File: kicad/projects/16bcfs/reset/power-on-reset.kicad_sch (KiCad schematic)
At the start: 2 parts

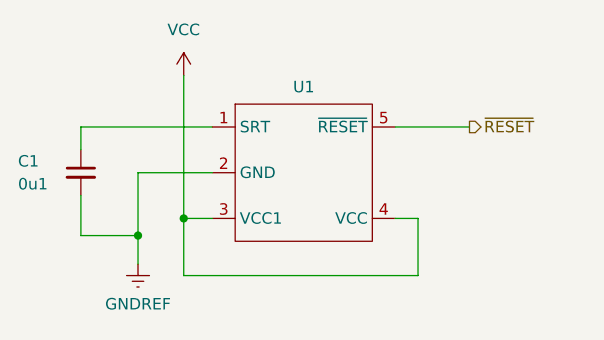
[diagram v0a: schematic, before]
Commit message: Added some debugging code
This is still not working.  I will need to revamp the reset routines for
the emulator to get this to work properly.  Everything will need an
initial state on construction and a `reset()` routine to place
everything into a proper state.  This in itself will be a major change.
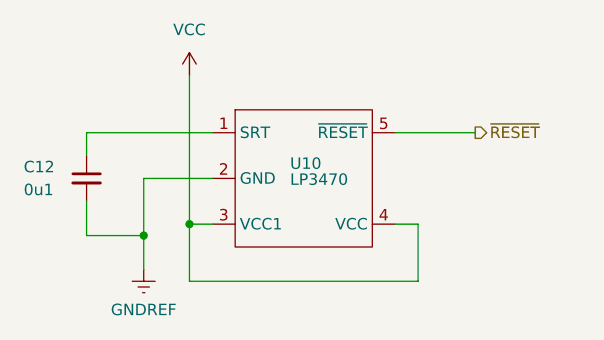
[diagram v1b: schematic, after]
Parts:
- U10: renamed from U1; value ~ -> LP3470
- renumbered C1 to C12
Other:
- moved on the sheet: C12, U10
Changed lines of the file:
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@@
     (comment 1 "Adam Clark (@eryjus)")
   )
-  (junction (at 132.715 104.775) (diameter 0) (color 0 0 0 0)
+  (junction (at 133.35 105.41) (diameter 0) (color 0 0 0 0)
   )
-  (junction (at 127.635 106.68) (diameter 0) (color 0 0 0 0)
+  (junction (at 128.27 106.68) (diameter 0) (color 0 0 0 0)
   )
-  (wire (pts (xy 121.285 106.68) (xy 127.635 106.68))
+  (wire (pts (xy 121.92 106.68) (xy 128.27 106.68))
     (stroke (width 0) (type default))
   )
-  (wire (pts (xy 127.635 99.695) (xy 127.635 106.68))
+  (wire (pts (xy 128.27 100.33) (xy 128.27 106.68))
     (stroke (width 0) (type default))
   )
-  (wire (pts (xy 132.715 111.125) (xy 132.715 104.775))
+  (wire (pts (xy 133.35 111.76) (xy 133.35 105.41))
     (stroke (width 0) (type default))
   )
-  (wire (pts (xy 132.715 104.775) (xy 135.89 104.775))
+  (wire (pts (xy 133.35 105.41) (xy 135.89 105.41))
     (stroke (width 0) (type default))
   )
-  (wire (pts (xy 121.285 102.235) (xy 121.285 106.68))
+  (wire (pts (xy 121.92 102.87) (xy 121.92 106.68))
     (stroke (width 0) (type default))
   )
-  (wire (pts (xy 164.465 94.615) (xy 156.21 94.615))
+  (wire (pts (xy 165.1 95.25) (xy 156.21 95.25))
     (stroke (width 0) (type default))
   )
-  (wire (pts (xy 132.715 88.9) (xy 132.715 104.775))
+  (wire (pts (xy 133.35 88.9) (xy 133.35 105.41))
     (stroke (width 0) (type default))
   )
-  (wire (pts (xy 135.89 94.615) (xy 121.285 94.615))
+  (wire (pts (xy 135.89 95.25) (xy 121.92 95.25))
     (stroke (width 0) (type default))
   )
-  (wire (pts (xy 158.75 111.125) (xy 132.715 111.125))
+  (wire (pts (xy 158.75 111.76) (xy 133.35 111.76))
     (stroke (width 0) (type default))
   )
-  (wire (pts (xy 127.635 106.68) (xy 127.635 109.855))
+  (wire (pts (xy 128.27 106.68) (xy 128.27 110.49))
     (stroke (width 0) (type default))
   )
-  (wire (pts (xy 156.21 104.775) (xy 158.75 104.775))
+  (wire (pts (xy 156.21 105.41) (xy 158.75 105.41))
     (stroke (width 0) (type default))
   )
-  (wire (pts (xy 135.89 99.695) (xy 127.635 99.695))
+  (wire (pts (xy 135.89 100.33) (xy 128.27 100.33))
     (stroke (width 0) (type default))
   )
-  (wire (pts (xy 121.285 94.615) (xy 121.285 97.155))
+  (wire (pts (xy 121.92 95.25) (xy 121.92 97.79))
     (stroke (width 0) (type default))
   )
-  (wire (pts (xy 158.75 104.775) (xy 158.75 111.125))
+  (wire (pts (xy 158.75 105.41) (xy 158.75 111.76))
     (stroke (width 0) (type default))
   )
-  (hierarchical_label "~{RESET}" (shape output) (at 164.465 94.615 0) (fields_autoplaced)
+  (hierarchical_label "~{RESET}" (shape output) (at 165.1 95.25 0) (fields_autoplaced)
     (effects (font (size 1.27 1.27)) (justify left))
   )
-  (symbol (lib_id "eryjus:LP3470A") (at 146.05 99.695 0) (unit 1)
-    (in_bom yes) (on_board yes) (dnp no) (fields_autoplaced)
-    (property "Reference" "U1" (at 146.05 90.17 0)
-      (effects (font (size 1.27 1.27)))
+  (symbol (lib_id "eryjus:LP3470A") (at 146.05 100.33 0) (unit 1)
+    (in_bom yes) (on_board yes) (dnp no)
+    (property "Reference" "U10" (at 144.526 98.679 0)
+      (effects (font (size 1.27 1.27)) (justify left))
     )
-    (property "Value" "~" (at 146.05 99.695 0)
-      (effects (font (size 1.27 1.27)))
+    (property "Value" "LP3470" (at 144.526 100.457 0)
+      (effects (font (size 1.27 1.27)) (justify left))
     )
-    (property "Footprint" "" (at 146.05 99.695 0)
+    (property "Footprint" "" (at 146.05 100.33 0)
       (effects (font (size 1.27 1.27)) hide)
     )
-    (property "Datasheet" "" (at 146.05 99.695 0)
+    (property "Datasheet" "" (at 146.05 100.33 0)
       (effects (font (size 1.27 1.27)) hide)
     )
@@
       (project "reset"
         (path "/d0ae44e5-d74e-4df6-bf3d-e0535c5a7785/bb61786e-9a6f-43f1-ab22-9986a9d0f989"
-          (reference "U1") (unit 1)
+          (reference "U10") (unit 1)
         )
       )
     )
   )
-  (symbol (lib_id "Device:C_Small") (at 121.285 99.695 0) (unit 1)
+  (symbol (lib_id "Device:C_Small") (at 121.92 100.33 0) (unit 1)
     (in_bom yes) (on_board yes) (dnp no)
-    (property "Reference" "C1" (at 114.3 98.425 0)
+    (property "Reference" "C12" (at 114.935 99.06 0)
       (effects (font (size 1.27 1.27)) (justify left))
     )
-    (property "Value" "0u1" (at 114.3 100.965 0)
+    (property "Value" "0u1" (at 114.935 101.6 0)
       (effects (font (size 1.27 1.27)) (justify left))
     )
-    (property "Footprint" "" (at 121.285 99.695 0)
+    (property "Footprint" "" (at 121.92 100.33 0)
       (effects (font (size 1.27 1.27)) hide)
     )
-    (property "Datasheet" "~" (at 121.285 99.695 0)
+    (property "Datasheet" "~" (at 121.92 100.33 0)
       (effects (font (size 1.27 1.27)) hide)
     )
@@
       (project "reset"
         (path "/d0ae44e5-d74e-4df6-bf3d-e0535c5a7785/bb61786e-9a6f-43f1-ab22-9986a9d0f989"
-          (reference "C1") (unit 1)
+          (reference "C12") (unit 1)
         )
       )
     )
   )
-  (symbol (lib_id "power:VCC") (at 132.715 88.9 0) (mirror y) (unit 1)
+  (symbol (lib_id "power:VCC") (at 133.35 88.9 0) (mirror y) (unit 1)
     (in_bom yes) (on_board yes) (dnp no)
-    (property "Reference" "#PWR06" (at 132.715 92.71 0)
+    (property "Reference" "#PWR014" (at 133.35 92.71 0)
       (effects (font (size 1.27 1.27)) hide)
     )
-    (property "Value" "VCC" (at 132.715 83.82 0)
+    (property "Value" "VCC" (at 133.35 83.82 0)
       (effects (font (size 1.27 1.27)))
     )
-    (property "Footprint" "" (at 132.715 88.9 0)
+    (property "Footprint" "" (at 133.35 88.9 0)
       (effects (font (size 1.27 1.27)) hide)
     )
-    (property "Datasheet" "" (at 132.715 88.9 0)
+    (property "Datasheet" "" (at 133.35 88.9 0)
       (effects (font (size 1.27 1.27)) hide)
     )
@@
       (project "reset"
         (path "/d0ae44e5-d74e-4df6-bf3d-e0535c5a7785/bb61786e-9a6f-43f1-ab22-9986a9d0f989"
-          (reference "#PWR06") (unit 1)
+          (reference "#PWR014") (unit 1)
         )
       )
     )
   )
-  (symbol (lib_id "power:GNDREF") (at 127.635 109.855 0) (unit 1)
+  (symbol (lib_id "power:GNDREF") (at 128.27 110.49 0) (unit 1)
     (in_bom yes) (on_board yes) (dnp no) (fields_autoplaced)
-    (property "Reference" "#PWR05" (at 127.635 116.205 0)
+    (property "Reference" "#PWR015" (at 128.27 116.84 0)
       (effects (font (size 1.27 1.27)) hide)
     )
-    (property "Value" "GNDREF" (at 127.635 114.3 0)
+    (property "Value" "GNDREF" (at 128.27 114.935 0)
       (effects (font (size 1.27 1.27)))
     )
-    (property "Footprint" "" (at 127.635 109.855 0)
+    (property "Footprint" "" (at 128.27 110.49 0)
       (effects (font (size 1.27 1.27)) hide)
     )
-    (property "Datasheet" "" (at 127.635 109.855 0)
+    (property "Datasheet" "" (at 128.27 110.49 0)
       (effects (font (size 1.27 1.27)) hide)
     )
@@
       (project "reset"
         (path "/d0ae44e5-d74e-4df6-bf3d-e0535c5a7785/bb61786e-9a6f-43f1-ab22-9986a9d0f989"
-          (reference "#PWR05") (unit 1)
+          (reference "#PWR015") (unit 1)
         )
       )

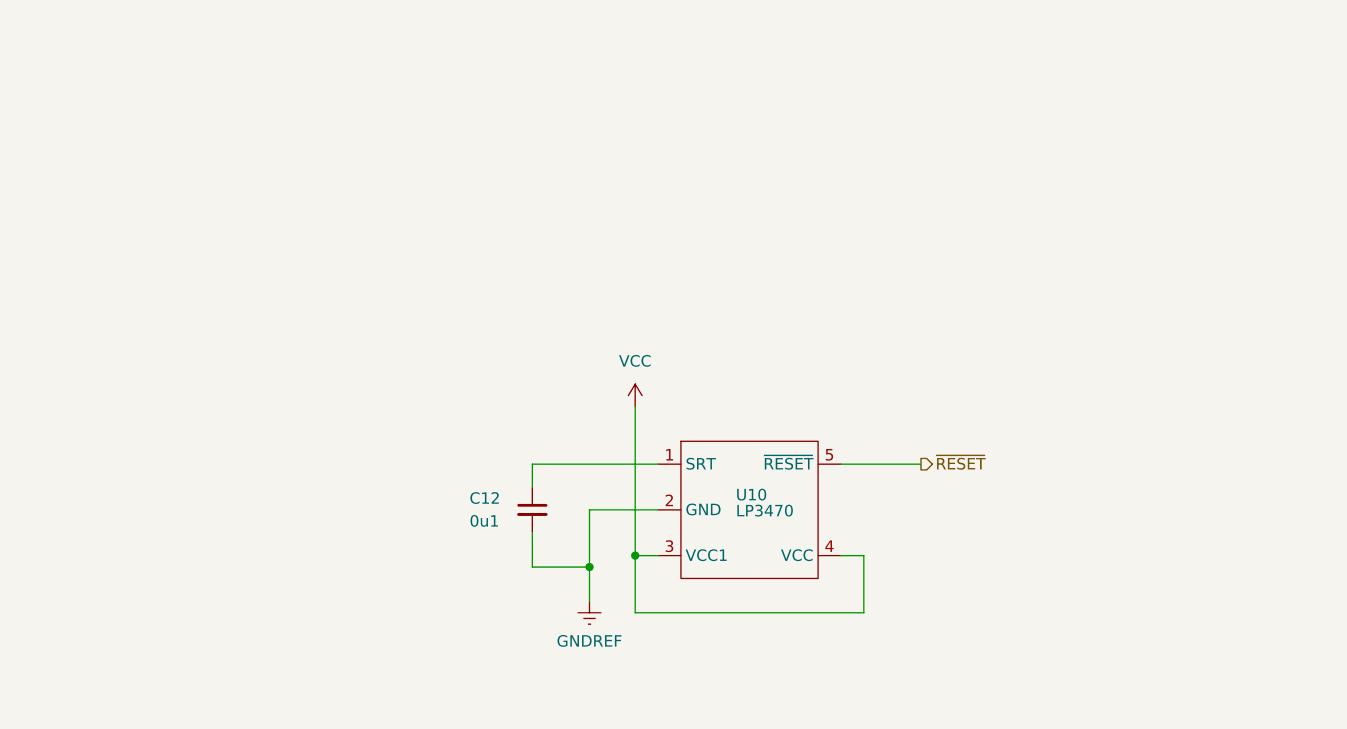
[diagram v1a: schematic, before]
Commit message: Address some issues with the Reset Logic
There were a couple of fixes.  One in relation to how the 74xx123 IC was
emulated and others to the schematic to address issues in real life in
the breadboard prototype.
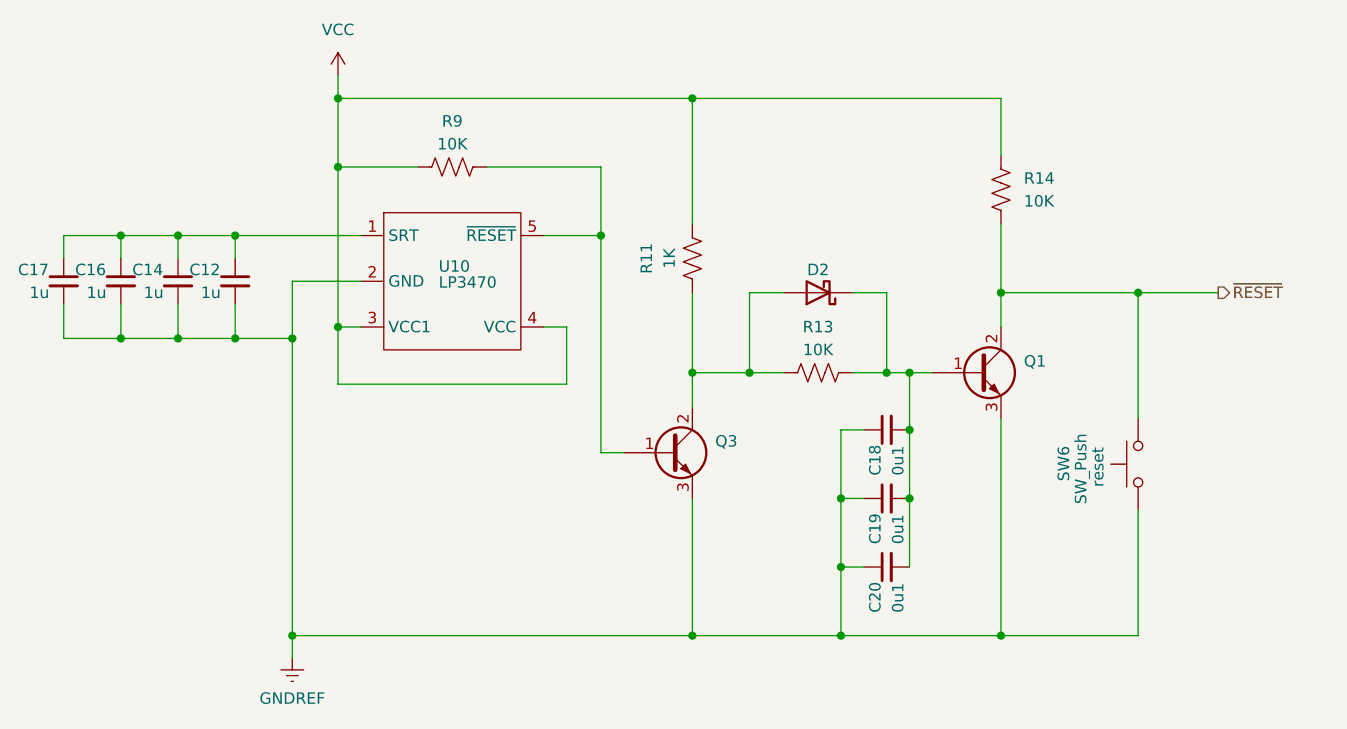
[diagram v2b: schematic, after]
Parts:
- added C14, C16, C17: 1u, symbol Device:C_Small
- added C18, C19, C20: 0u1, symbol Device:C_Small
- added D2: D_Schottky, symbol Device:D_Schottky
- added Q1, Q3: Q_NPN_BCE, symbol Device:Q_NPN_BCE
- added R11: 1K, symbol Device:R_US
- added R13, R14, R9: 10K, symbol Device:R_US
- added SW6: SW_Push, symbol Switch:SW_Push
- C12: value 0u1 -> 1u
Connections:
- net GNDREF: now also C14.2, C16.2, C17.2, C18.1, C19.1, C20.1, Q1.3 (E), Q3.3 (E), SW6.1
- net VCC: now also R11.2, R14.1, R9.1
- net ~{RESET}: now also Q1.2 (C), R14.2, SW6.2; no longer U10.5 (~{RESET})
- net at C12.1, U10.1 (SRT): now also C14.1, C16.1, C17.1
- new net: D2.2 (A), Q3.2 (C), R11.1, R13.1
- new net: Q3.1 (B), R9.2, U10.5 (~{RESET})
- new net: C18.2, C19.2, C20.2, D2.1 (K), Q1.1 (B), R13.2
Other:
- moved on the sheet: C12, U10
